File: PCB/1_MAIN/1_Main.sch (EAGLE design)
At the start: 39 parts, among them IC10 FT232RL, IC11 NCP1117ST33, IC7 MAX14932, IC8 MAX14932, IC9 MAX14932, Q1 IRF7416, X14 ALLSERIALMM, X2 MINI-USB-32005-201, X3 AKL18X-04W

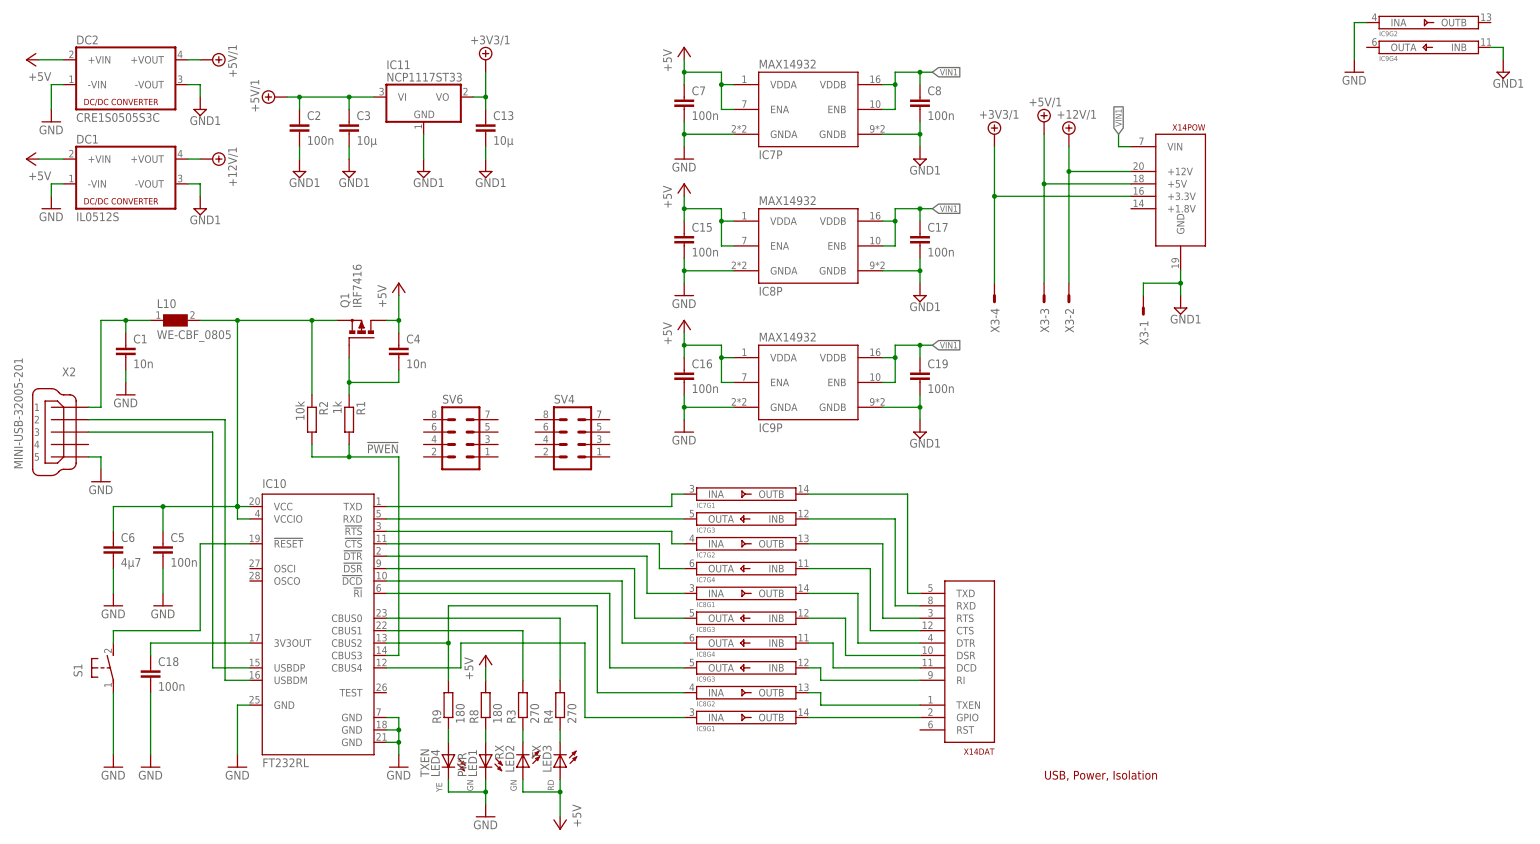
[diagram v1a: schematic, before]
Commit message: Improve lib
Route RS232 board
Route TTL board
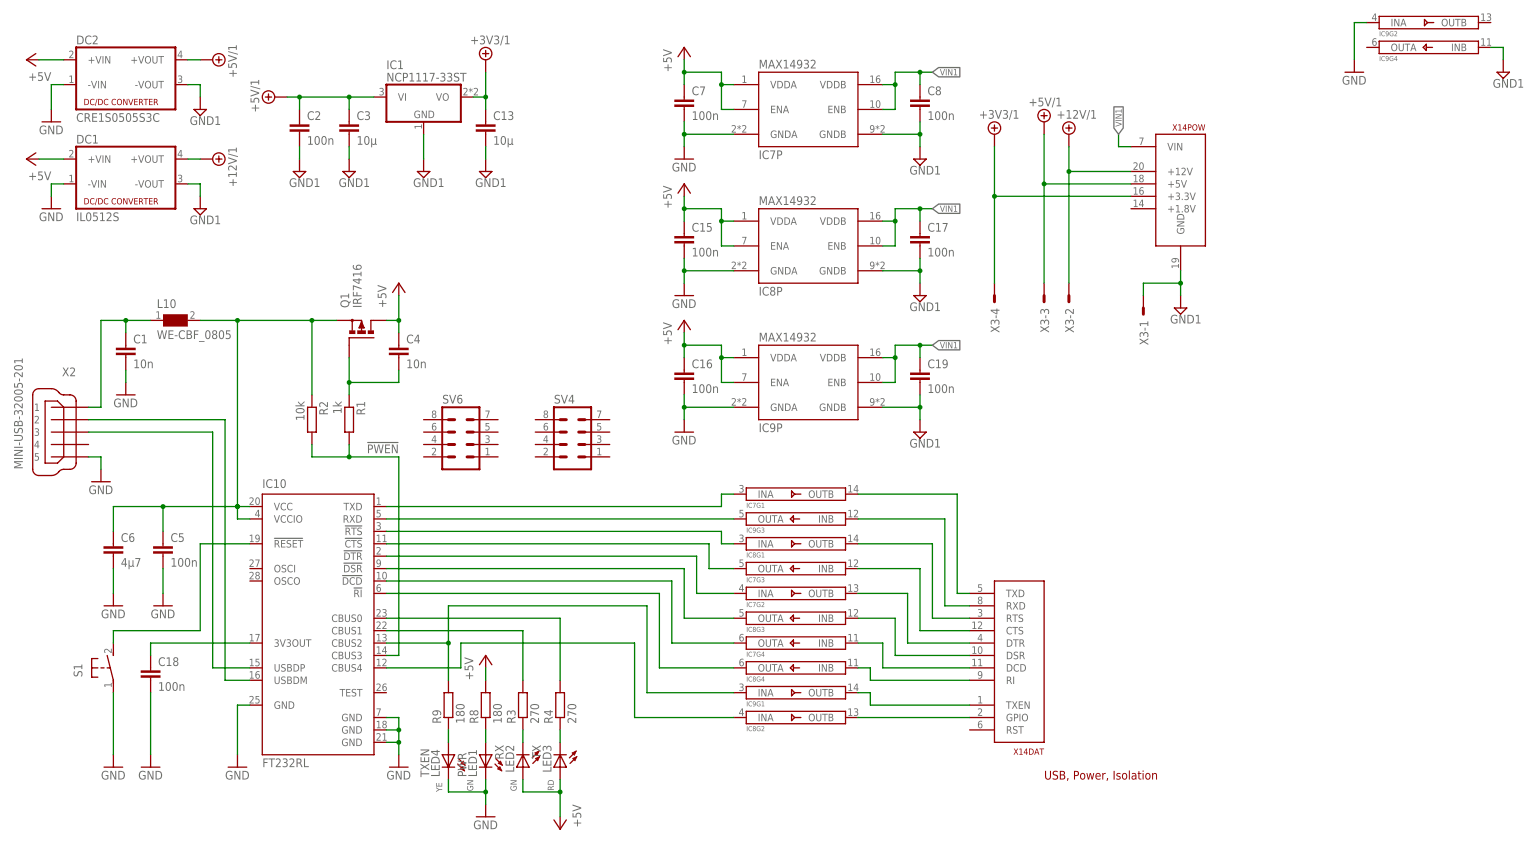
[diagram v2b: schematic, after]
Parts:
- removed IC11: NCP1117ST33, linear:MCP1703CB
- added IC1: NCP1117-33ST, linear:NCP1117-33ST
- LED1, LED2, LED3, LED4: device led:LEDCHIPLED_0805 -> led:LEDCHIPLED_0603
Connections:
- net +3V3/1: now also IC1.VO; no longer IC11.VO
- net +5V/1: now also IC1.VI; no longer IC11.VI
- net GND1: now also IC1.GND; no longer IC11.GND
- net N$13: now also IC8G2.INA; no longer IC9G1.INA
- net N$20: now also IC9G3.OUTA; no longer IC7G3.OUTA
- net N$29: now also IC8G1.INA; no longer IC7G2.INA
- net N$3: now also IC9G1.INA; no longer IC8G2.INA
- net N$32: now also IC7G3.OUTA; no longer IC7G4.OUTA
- net N$33: now also IC7G2.INA; no longer IC8G1.INA
- net N$35: now also IC7G4.OUTA; no longer IC8G4.OUTA
- net N$36: now also IC8G4.OUTA; no longer IC9G3.OUTA
- net N$81: now also IC9G3.INB; no longer IC7G3.INB
- net N$82: now also IC8G1.OUTB; no longer IC7G2.OUTB
- net N$83: now also IC7G3.INB; no longer IC7G4.INB
- net N$84: now also IC7G2.OUTB; no longer IC8G1.OUTB
- net N$86: now also IC7G4.INB; no longer IC8G4.INB
- net N$87: now also IC8G4.INB; no longer IC9G3.INB
- net N$88: now also IC9G1.OUTB; no longer IC8G2.OUTB
- net N$89: now also IC8G2.OUTB; no longer IC9G1.OUTB
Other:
- moved on the sheet: IC7G1, IC7G2, IC7G3, IC7G4, IC8G1, IC8G2, IC8G3, IC8G4, IC9G1, IC9G3, X14DAT
